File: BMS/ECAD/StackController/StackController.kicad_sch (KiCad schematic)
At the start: 10 parts, among them U1 TLE9012, U2 TMUX1309A, U3 TMUX1309A

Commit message: started stack controller design
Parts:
- removed R3: 866kR 0,1% 25ppm/C, Resistor_SMD:R_0603_1608Metric, symbol Device:R
- removed R4: 887kR 0,1% 25ppm/C, Resistor_SMD:R_0603_1608Metric, symbol Device:R
- removed R5: 909kR 0,1% 25ppm/C, Resistor_SMD:R_0603_1608Metric, symbol Device:R
- removed R6: 931kR 0,1% 25ppm/C, Resistor_SMD:R_0603_1608Metric, symbol Device:R
- removed U2, U3: TMUX1309A, symbol EKartParts:TMUX1309A
- added C1, C11, C2, C3, C4, C5: 10nC 16V, Capacitor_SMD:C_0603_1608Metric, symbol Device:C
- added C10: 10uC 16V, Capacitor_SMD:C_0805_2012Metric, symbol Device:C
- added C12, C13: 100nC 16V, Capacitor_SMD:C_0603_1608Metric, symbol Device:C
- added C14: 330nC 16V, Capacitor_SMD:C_0603_1608Metric, symbol Device:C
- added C51: 1nC 16V, Capacitor_SMD:C_0603_1608Metric, symbol Device:C
- added C52: 1nC 100V, Capacitor_SMD:C_0603_1608Metric, symbol Device:C
- added C53: 100nC 100V, Capacitor_SMD:C_0603_1608Metric, symbol Device:C
- added C56, C57, C58, C59, C60, C61, C62, C63: 1nC 1000V, Capacitor_SMD:C_1206_3216Metric, symbol Device:C
- added C6, C7, C8, C9: 10uC 16V, Capacitor_SMD:C_0603_1608Metric, symbol Device:C
- added Error1: LED Red, LED_SMD:LED_0805_2012Metric_Pad1.15x1.40mm_HandSolder, symbol Device:LED
- added Error2, Error3, Error4: LED Green, LED_SMD:LED_0805_2012Metric_Pad1.15x1.40mm_HandSolder, symbol Device:LED
- added F1, F10, F11, F12, F13, F2, F3, F4, F5, F6, F7, F8, F9: 1A, Fuse:Fuse_0603_1608Metric, symbol Device:Fuse
- added Q1202: BC846, Package_TO_SOT_SMD:SOT-23, symbol Transistor_BJT:BC846
- added R10, R11, R12, R8, R9: 100R 0,1% 25ppm/C, Resistor_SMD:R_0603_1608Metric, symbol Device:R
- added R13: 100R, Resistor_SMD:R_0603_1608Metric, symbol Device:R
- added R14: 1kR, Resistor_SMD:R_0603_1608Metric, symbol Device:R
- added R15, R16, R51: 10kR, Resistor_SMD:R_0603_1608Metric, symbol Device:R
- added R41, R42: 10R, Resistor_SMD:R_2512_6332Metric, symbol Device:R
- added R43, R46: 5.1R, Resistor_SMD:R_2512_6332Metric, symbol Device:R
- added R47, R48, R49, R50: 39R, Resistor_SMD:R_0603_1608Metric, symbol Device:R
- added R52: 330R, Resistor_SMD:R_0603_1608Metric, symbol Device:R
- added R53: 10kR, Resistor_SMD:R_0805_2012Metric, symbol Device:R
- added R54: 270R, Resistor_SMD:R_0603_1608Metric, symbol Device:R
- added R55: 62R, Resistor_SMD:R_0603_1608Metric, symbol Device:R
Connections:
- net GND: now also U1.15 (GND), U1.22 (GND), U1.49 (EP), C10.2, C11.2, C12.2, C13.2, C14.2, C51.2, C52.2, C53.1, C58.2, C59.2, C6.2, C62.2, C63.2, C7.2, C8.2, C9.2, Error2.1 (K), Error3.1 (K), Error4.1 (K), F13.1, Q1202.2 (E), R13.1, R14.1, R15.1, R16.1, R41.1
- net TMP0: now also C10.1, R12.1
- net TMP1: now also C9.1, R11.1
- net TMP2: now also C8.1, R10.1
- net TMP3: now also C7.1, R9.1
- net at R1.2, U1.28 (GPIO/UART_LS): now also R15.2
- net at R2.2, U1.29 (GPIO1/UART_HS): now also R16.2
- net Balancing_6/G: now reaches U1.1 (G5)
- net Balancing_10/U-1: now reaches U1.10 (U1)
- net Balancing_11/G: now reaches U1.11 (G0)
- net Balancing_11/U-1: now reaches U1.12 (U0)
- net Balancing_11/U-1: now also C51.1, R41.2
- net at U1.13 (TMP4): now also C5.1, R8.2; no longer R7.2
- net at U1.14 (TMP3): now also C4.1, R9.2
- net at U1.16 (TMP2): now also C3.1, R10.2
- net at U1.17 (TMP1): now also C2.1, R11.2
- net at U1.18 (TMP0): now also C1.1, R12.2
- net TPM_GND: now reaches U1.19 (TMP_GND)
- net TPM_GND: now also C1.2, C11.1, C2.2, C3.2, C4.2, C5.2, R13.2
- net Balancing_6/U-1: now reaches U1.2 (U5)
- net at U1.23 (IFL_L): now also R49.2
- net at U1.24 (IFL_H): now also R50.2
- net at U1.25 (IFH_H): now also R47.2
- net at U1.26 (IFH_L): now also R48.2
- net +2,5V: now reaches U1.27 (VDDC)
- net +2,5V: now also C14.1, R55.1
- net Balancing_7/G: now reaches U1.3 (G4)
- net +3.45V: now reaches U1.30 (VIO)
- net +3.45V: now also U1.31 (VregOut_VDDA), C13.1, R52.1, R54.1
- net at U1.33 (ERR): now also R51.2
- net VStack: now reaches U1.34 (VS)
- net VStack: now also C12.1, R46.1, R53.1
- net at U1.35 (U12P): now also R43.1
- net Balancing_0/U: now reaches U1.36 (U12)
- net Balancing_0/G: now reaches U1.37 (G11)
- net Balancing_0/U-1: now reaches U1.38 (U11)
- net Balancing_1/G: now reaches U1.39 (G10)
- net Balancing_7/U-1: now reaches U1.4 (U4)
- net Balancing_1/U-1: now reaches U1.40 (U10)
- net Balancing_2/G: now reaches U1.41 (G9)
- net Balancing_2/U-1: now reaches U1.42 (U9)
- net Balancing_3/G: now reaches U1.43 (G8)
- net Balancing_3/U-1: now reaches U1.44 (U8)
- net Balancing_4/G: now reaches U1.45 (G7)
- net Balancing_5/U: now reaches U1.46 (U7)
- net Balancing_5/G: now reaches U1.47 (G6)
- net Balancing_5/U-1: now reaches U1.48 (U6)
- net Balancing_8/G: now reaches U1.5 (G3)
- net Balancing_8/U-1: now reaches U1.6 (U3)
- net Balancing_9/G: now reaches U1.7 (G2)
- net Balancing_10/U: now reaches U1.8 (U2)
- net Balancing_10/G: now reaches U1.9 (G1)
- new net: C61.2, C63.1, R49.1
- new net: C57.1, C58.1, R48.1
- new net: Q1202.1 (B), R14.2, R51.1
- new net: Error1.1 (K), Q1202.3 (C)
- new net: Error1.2 (A), R52.2
- new net: C6.1, R7.2, R8.1
- new net: Error3.2 (A), R54.2
- new net: Error4.2 (A), R55.2
- new net: C53.2, R42.1, R43.2
- new net: Error2.2 (A), R53.2
- new net: C60.2, C62.1, R50.1
- new net: C56.1, C59.1, R47.1
- new net Balancing_0/V+_Cell: C52.1, F12.2, R42.2, R46.2
- new net Balancing_1/V+_Cell: F11.2
- new net Balancing_10/V+_Cell: F6.1
- new net Balancing_11/V+_Cell: F7.1
- new net Balancing_2/V+_Cell: F10.2
- new net Balancing_3/V+_Cell: F9.2
- new net Balancing_4/V+_Cell: F8.2
- new net Balancing_5/V+_Cell: F1.1
- new net Balancing_6/V+_Cell: F2.1
- new net Balancing_7/V+_Cell: F3.1
- new net Balancing_8/V+_Cell: F4.1
- new net Balancing_9/V+_Cell: F5.1
- new net Bot_IsoSPI_H: C60.1
- new net Bot_IsoSPI_L: C61.1
- new net C0: F7.2
- new net C0_N: F13.2
- new net C1: F6.2
- new net C10: F11.1
- new net C11: F12.1
- new net C2: F5.2
- new net C3: F4.2
- new net C4: F3.2
- new net C5: F2.2
- new net C6: F1.2
- new net C7: F8.1
- new net C8: F9.1
- new net C9: F10.1
- new net Top_IsoSPI_H: C56.2
- new net Top_IsoSPI_L: C57.2
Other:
- added sheet Balancing_0 (Balancing.kicad_sch)
- added sheet Balancing_1 (Balancing.kicad_sch)
- added sheet Balancing_10 (Balancing.kicad_sch)
- added sheet Balancing_11 (Balancing.kicad_sch)
- added sheet Balancing_2 (Balancing.kicad_sch)
- added sheet Balancing_3 (Balancing.kicad_sch)
- added sheet Balancing_4 (Balancing.kicad_sch)
- added sheet Balancing_5 (Balancing.kicad_sch)
- added sheet Balancing_6 (Balancing.kicad_sch)
- added sheet Balancing_7 (Balancing.kicad_sch)
- added sheet Balancing_8 (Balancing.kicad_sch)
- added sheet Balancing_9 (Balancing.kicad_sch)
- added sheet NTC_MUX (NTC_MUX.kicad_sch)
- moved on the sheet: R1, R2, R7

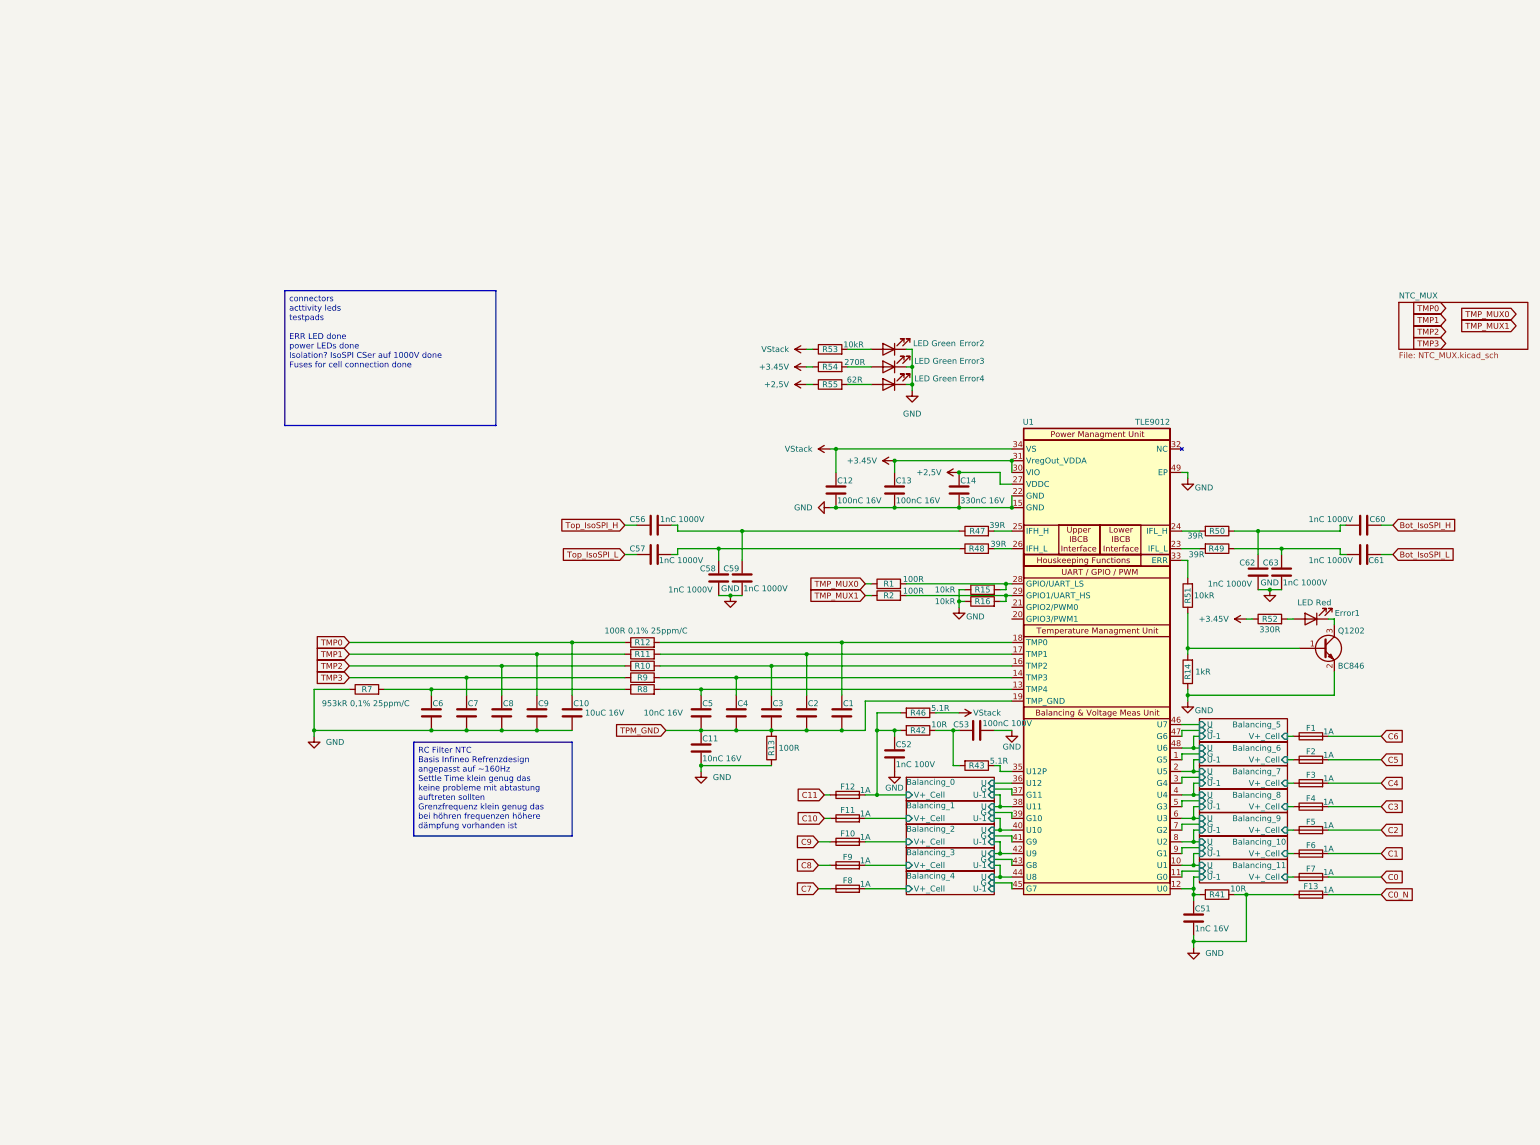
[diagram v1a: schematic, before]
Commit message: finish V09 of stack controller and HV indicator
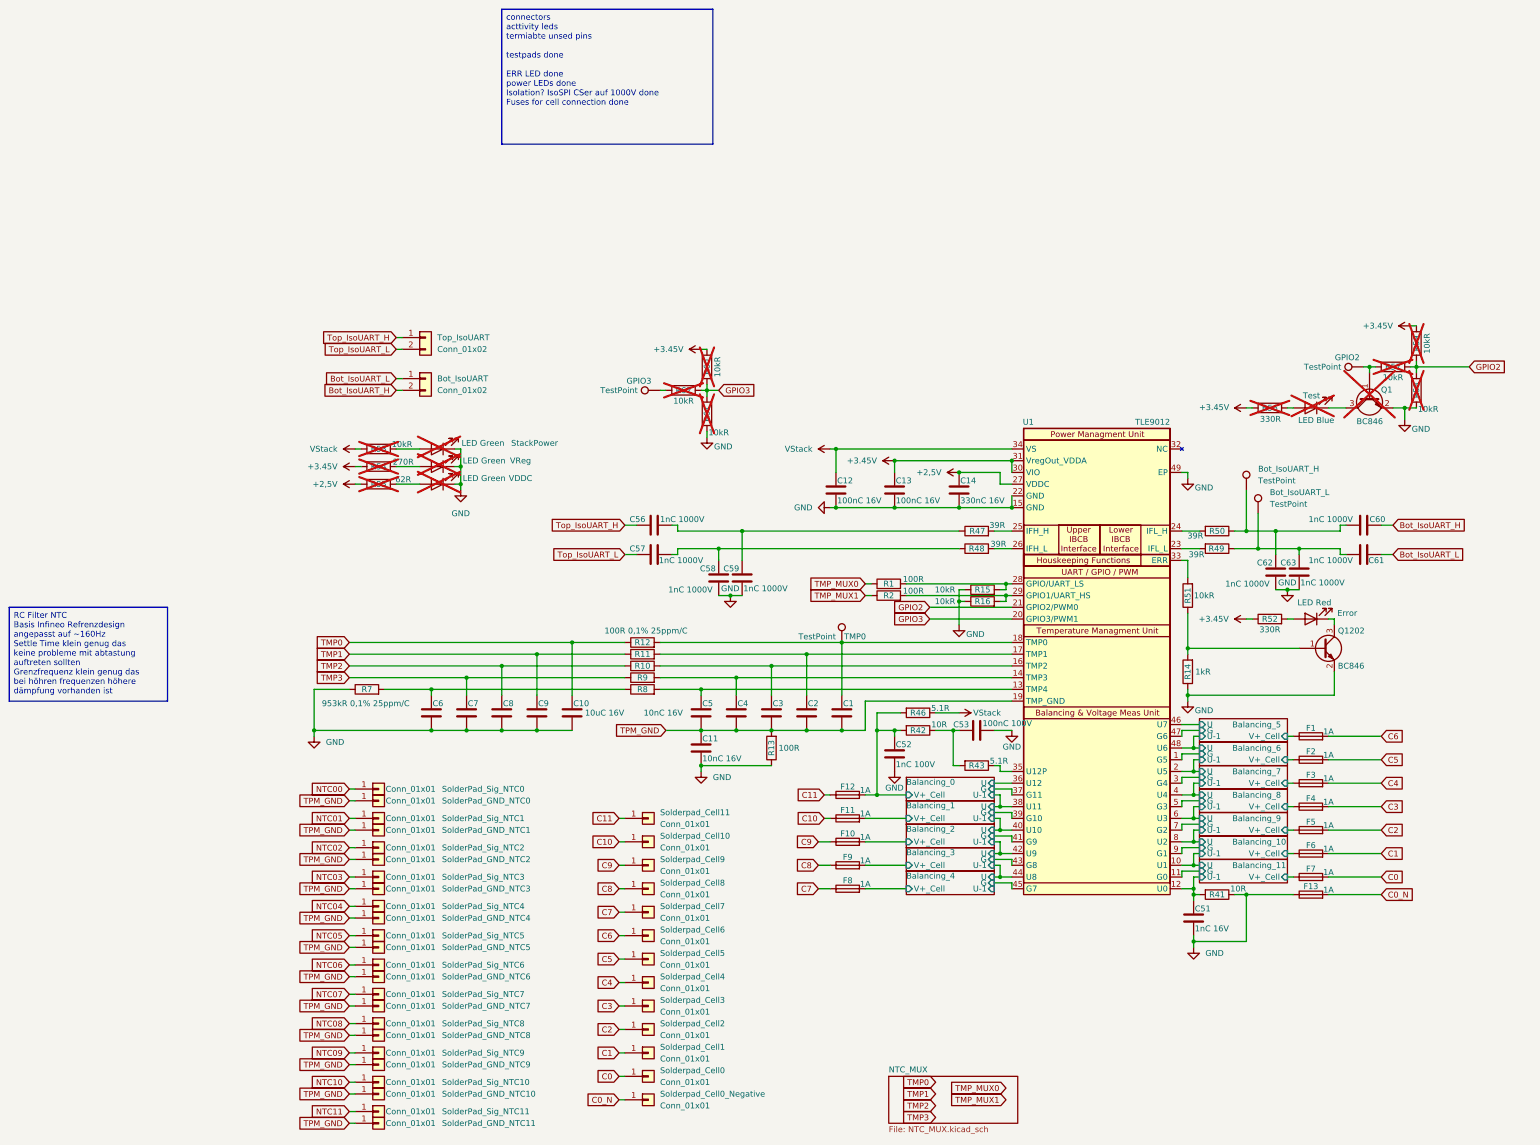
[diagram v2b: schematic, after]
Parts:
- added Bot_IsoUART, Top_IsoUART: Conn_01x02, Connector_Molex:Molex_Micro-Fit_3.0_43045-0200_2x01_P3.00mm_Horizontal, symbol Connector_Generic:Conn_01x02
- added Bot_IsoUART_H, Bot_IsoUART_L, GPIO2, GPIO3, TMP0: TestPoint, TestPoint:TestPoint_Loop_D1.80mm_Drill1.0mm_Beaded, symbol Connector:TestPoint
- added Q1: BC846, Package_TO_SOT_SMD:SOT-23, symbol Transistor_BJT:BC846
- added R56: 330R, Resistor_SMD:R_0603_1608Metric, symbol Device:R
- added R57, R58, R59, R60, R61, R62: 10kR, Resistor_SMD:R_0603_1608Metric, symbol Device:R
- added SolderPad_GND_NTC0, SolderPad_GND_NTC1, SolderPad_GND_NTC10, SolderPad_GND_NTC11, SolderPad_GND_NTC2, SolderPad_GND_NTC3, SolderPad_GND_NTC4, SolderPad_GND_NTC5, SolderPad_GND_NTC6, SolderPad_GND_NTC7, SolderPad_GND_NTC8, SolderPad_GND_NTC9, SolderPad_Sig_NTC0, SolderPad_Sig_NTC1, SolderPad_Sig_NTC10, SolderPad_Sig_NTC11, SolderPad_Sig_NTC2, SolderPad_Sig_NTC3, SolderPad_Sig_NTC4, SolderPad_Sig_NTC5, SolderPad_Sig_NTC6, SolderPad_Sig_NTC7, SolderPad_Sig_NTC8, SolderPad_Sig_NTC9: Conn_01x01, TestPoint:TestPoint_Pad_D1.5mm, symbol Connector_Generic:Conn_01x01
- added Solderpad_Cell0, Solderpad_Cell0_Negative, Solderpad_Cell1, Solderpad_Cell10, Solderpad_Cell11, Solderpad_Cell2, Solderpad_Cell3, Solderpad_Cell4, Solderpad_Cell5, Solderpad_Cell6, Solderpad_Cell7, Solderpad_Cell8, Solderpad_Cell9: Conn_01x01, TestPoint:TestPoint_Pad_D3.0mm, symbol Connector_Generic:Conn_01x01
- added Test: LED Blue, LED_SMD:LED_0805_2012Metric_Pad1.15x1.40mm_HandSolder, symbol Device:LED
- R53, R54, R55: now not fitted
- StackPower: renamed from Error2; now not fitted
- VDDC: renamed from Error4; now not fitted
- VReg: renamed from Error3; now not fitted
- renumbered Error1 to Error
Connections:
- net +3.45V: now also R56.2, R59.2, R60.2
- net C0: now also Solderpad_Cell0.1 (Pin_1)
- net C0_N: now also Solderpad_Cell0_Negative.1 (Pin_1)
- net C1: now also Solderpad_Cell1.1 (Pin_1)
- net C10: now also Solderpad_Cell10.1 (Pin_1)
- net C11: now also Solderpad_Cell11.1 (Pin_1)
- net C2: now also Solderpad_Cell2.1 (Pin_1)
- net C3: now also Solderpad_Cell3.1 (Pin_1)
- net C4: now also Solderpad_Cell4.1 (Pin_1)
- net C5: now also Solderpad_Cell5.1 (Pin_1)
- net C6: now also Solderpad_Cell6.1 (Pin_1)
- net C7: now also Solderpad_Cell7.1 (Pin_1)
- net C8: now also Solderpad_Cell8.1 (Pin_1)
- net C9: now also Solderpad_Cell9.1 (Pin_1)
- net GND: now also Q1.2 (E), R58.1, R61.1
- net TPM_GND: now also SolderPad_GND_NTC0.1 (Pin_1), SolderPad_GND_NTC1.1 (Pin_1), SolderPad_GND_NTC10.1 (Pin_1), SolderPad_GND_NTC11.1 (Pin_1), SolderPad_GND_NTC2.1 (Pin_1), SolderPad_GND_NTC3.1 (Pin_1), SolderPad_GND_NTC4.1 (Pin_1), SolderPad_GND_NTC5.1 (Pin_1), SolderPad_GND_NTC6.1 (Pin_1), SolderPad_GND_NTC7.1 (Pin_1), SolderPad_GND_NTC8.1 (Pin_1), SolderPad_GND_NTC9.1 (Pin_1)
- net at C61.2, C63.1, R49.1: now also Bot_IsoUART_L.1
- net at C1.1, R12.2, U1.18 (TMP0): now also TMP0.1
- net at C60.2, C62.1, R50.1: now also Bot_IsoUART_H.1
- net GPIO3: now reaches U1.20 (GPIO3/PWM1)
- net GPIO3: now also R60.1, R61.2, R62.2
- net GPIO2: now reaches U1.21 (GPIO2/PWM0)
- net GPIO2: now also R57.2, R58.2, R59.1
- net Bot_IsoSPI_H renamed Bot_IsoUART_H
- net Bot_IsoUART_H: now also Bot_IsoUART.2 (Pin_2)
- net Bot_IsoSPI_L renamed Bot_IsoUART_L
- net Bot_IsoUART_L: now also Bot_IsoUART.1 (Pin_1)
- net Top_IsoSPI_H renamed Top_IsoUART_H
- net Top_IsoUART_H: now also Top_IsoUART.1 (Pin_1)
- net Top_IsoSPI_L renamed Top_IsoUART_L
- net Top_IsoUART_L: now also Top_IsoUART.2 (Pin_2)
- new net: GPIO2.1, Q1.1 (B), R57.1
- new net: Q1.3 (C), Test.1 (K)
- new net: GPIO3.1, R62.1
- new net: R56.1, Test.2 (A)
- new net NTC00: SolderPad_Sig_NTC0.1 (Pin_1)
- new net NTC01: SolderPad_Sig_NTC1.1 (Pin_1)
- new net NTC02: SolderPad_Sig_NTC2.1 (Pin_1)
- new net NTC03: SolderPad_Sig_NTC3.1 (Pin_1)
- new net NTC04: SolderPad_Sig_NTC4.1 (Pin_1)
- new net NTC05: SolderPad_Sig_NTC5.1 (Pin_1)
- new net NTC06: SolderPad_Sig_NTC6.1 (Pin_1)
- new net NTC07: SolderPad_Sig_NTC7.1 (Pin_1)
- new net NTC08: SolderPad_Sig_NTC8.1 (Pin_1)
- new net NTC09: SolderPad_Sig_NTC9.1 (Pin_1)
- new net NTC10: SolderPad_Sig_NTC10.1 (Pin_1)
- new net NTC11: SolderPad_Sig_NTC11.1 (Pin_1)
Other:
- moved on the sheet: C62, C63
